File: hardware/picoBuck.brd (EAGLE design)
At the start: 22.8 x 27.3 mm, 26 parts, among them U1 AL8805, U2 AL8805, U3 AL8805

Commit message: Tweaks on text positions.
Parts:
- removed JP1: (no value), SparkFun:SCREWTERMINAL-3.5MM-3_LOCK.007S
- added JP3, JP4: M022.54MM_SCREWTERM, SparkFun-Connectors:1X02_2.54_SCREWTERM
- moved LOGO2 41.7 mm to (20.7, 2.16), flipped to the bottom
- moved LOGO1 39.0 mm to (9.02, 24.1), flipped to the bottom
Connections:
- net CTRL_CH1: now also JP4.P1; no longer JP1.3
- net CTRL_CH2: now also JP3.P2; no longer JP1.2
- net CTRL_CH3: now also JP3.P1; no longer JP1.1
- net GND: now also JP4.P2
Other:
- board text added: "GND"

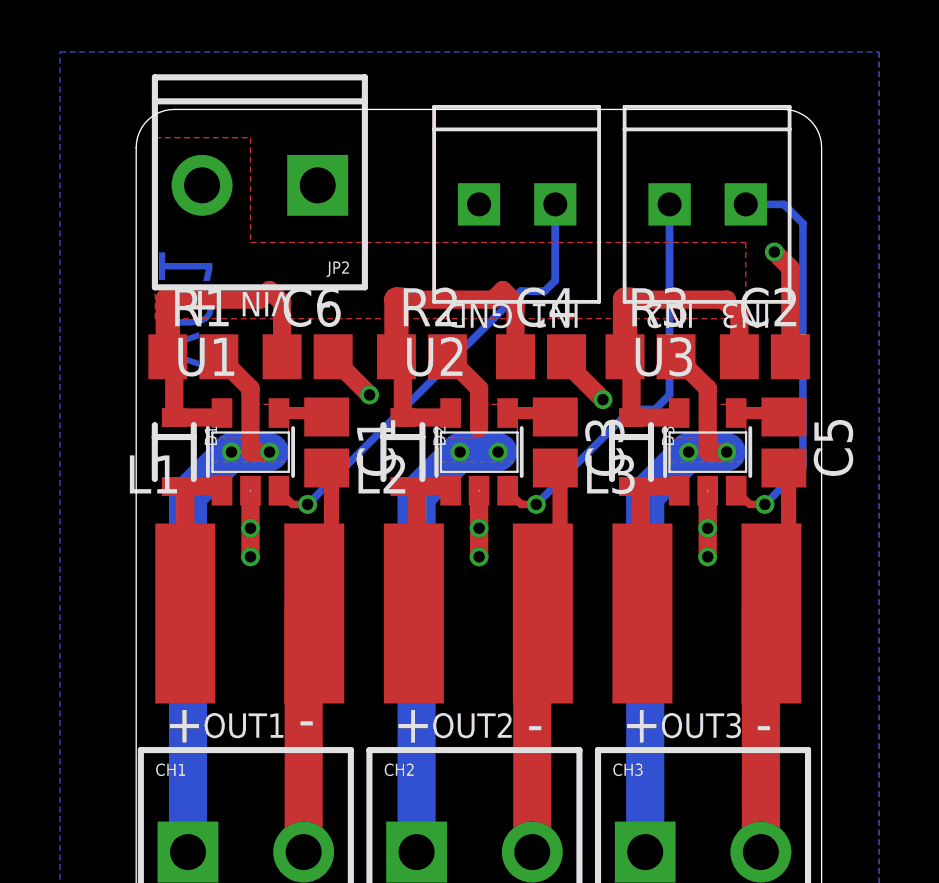
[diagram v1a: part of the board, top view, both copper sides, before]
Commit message: Update to v10, for release. Add .gitignore and README
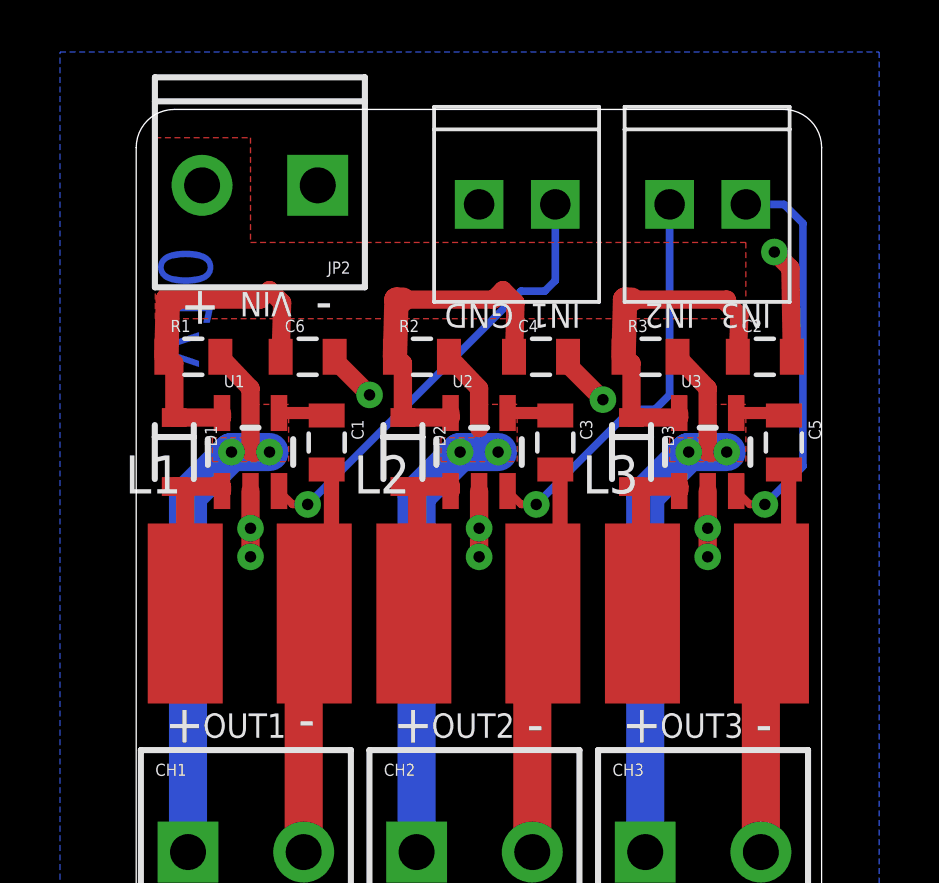
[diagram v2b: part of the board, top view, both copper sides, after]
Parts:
- C1, C2, C3, C4, C5, C6: device resistor:C0805 -> SparkFun-Capacitors:0805
- D1, D2, D3: device SparkFun:SOD-323 -> SparkFun-DiscreteSemi:SOD-323
- L1, L2, L3: value SRN6045 -> 33uH; device Protofusion:SRN6045 -> SparkFun-Passives:SRN6045
- R1, R2, R3: device resistor:R0805 -> SparkFun-Resistors:0805
- U1, U2, U3: value AL8805 -> (none); device Protofusion:SOT23-5 -> SparkFun-PowerIC:SOT23-5
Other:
- board text added: "v10"
- board text removed: "protofusion.org/picobuck"
- board text removed: "v01"

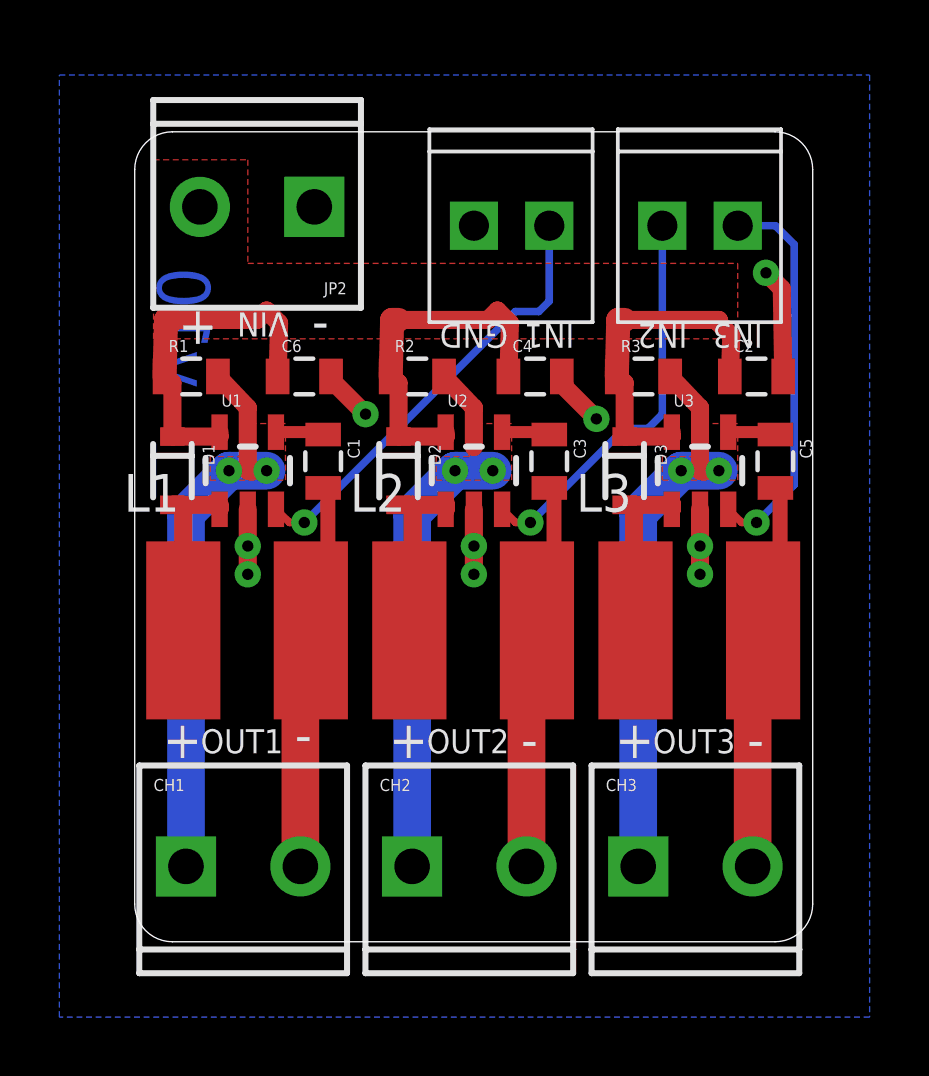
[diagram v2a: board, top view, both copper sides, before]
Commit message: Cosmetic tweaks
moved brd on grid, shrunk ground plane, other minor stuff
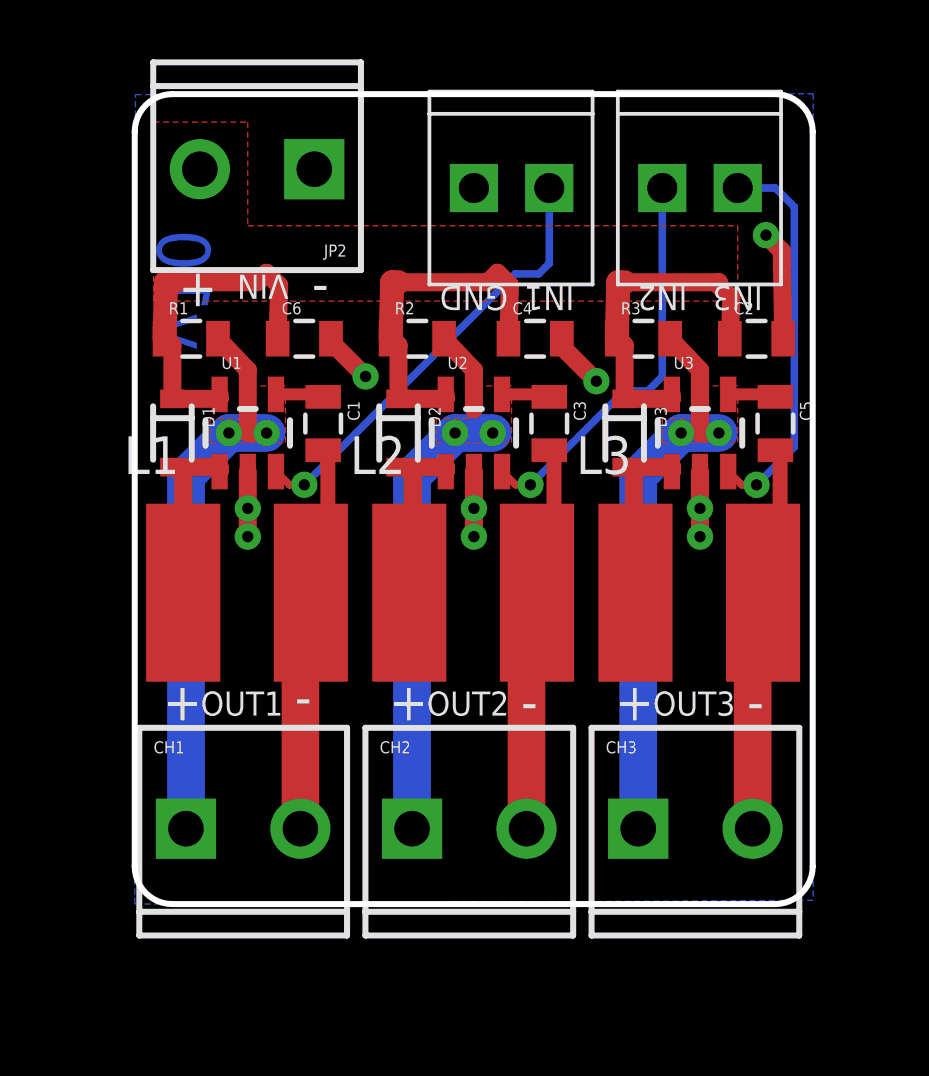
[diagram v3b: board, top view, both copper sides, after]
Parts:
- moved CH1 1.27 mm to (1.91, 2.54)
- moved CH2 1.27 mm to (9.53, 2.54)
- moved CH3 1.27 mm to (17.1, 2.54)
- moved LOGO2 1.27 mm to (20.7, 3.43)
- moved C1 1.27 mm to (6.35, 16.2)
- moved C2 1.27 mm to (21.0, 19.1)
- moved C3 1.27 mm to (14.0, 16.2)
- moved C4 1.27 mm to (13.5, 19.1)
- moved C5 1.27 mm to (21.6, 16.2)
- moved C6 1.27 mm to (5.71, 19.1)
- moved D1 1.27 mm to (1.27, 15.9)
- moved D2 1.27 mm to (8.89, 15.9)
- moved D3 1.27 mm to (16.5, 15.9)
- moved JP2 1.27 mm to (5.87, 24.8)
- moved JP3 1.27 mm to (17.8, 24.1)
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
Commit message: Production ready
panelized and added fiducials
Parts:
- added FID1, FID2: FIDUCIALUFIDUCIAL, SparkFun-Aesthetics:MICRO-FIDUCIAL
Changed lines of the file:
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@@
 <setting verticaltext="up"/>
 </settings>
-<grid distance="0.01" unitdist="inch" unit="inch" style="lines" multiple="1" display="yes" altdistance="0.001" altunitdist="inch" altunit="inch"/>
+<grid distance="0.05" unitdist="inch" unit="inch" style="lines" multiple="1" display="yes" altdistance="0.01" altunitdist="inch" altunit="inch"/>
 <layers>
 <layer number="1" name="Top" color="4" fill="1" visible="yes" active="yes"/>
@@
 <element name="JP3" library="SparkFun-Connectors" package="1X02_2.54_SCREWTERM" value="M022.54MM_SCREWTERM" x="17.78" y="24.13"/>
 <element name="JP4" library="SparkFun-Connectors" package="1X02_2.54_SCREWTERM" value="M022.54MM_SCREWTERM" x="11.43" y="24.13"/>
+<element name="FID1" library="SparkFun-Aesthetics" package="MICRO-FIDUCIAL" value="FIDUCIALUFIDUCIAL" x="3.81" y="1.016"/>
+<element name="FID2" library="SparkFun-Aesthetics" package="MICRO-FIDUCIAL" value="FIDUCIALUFIDUCIAL" x="20.828" y="25.908"/>
 </elements>
 <signals>

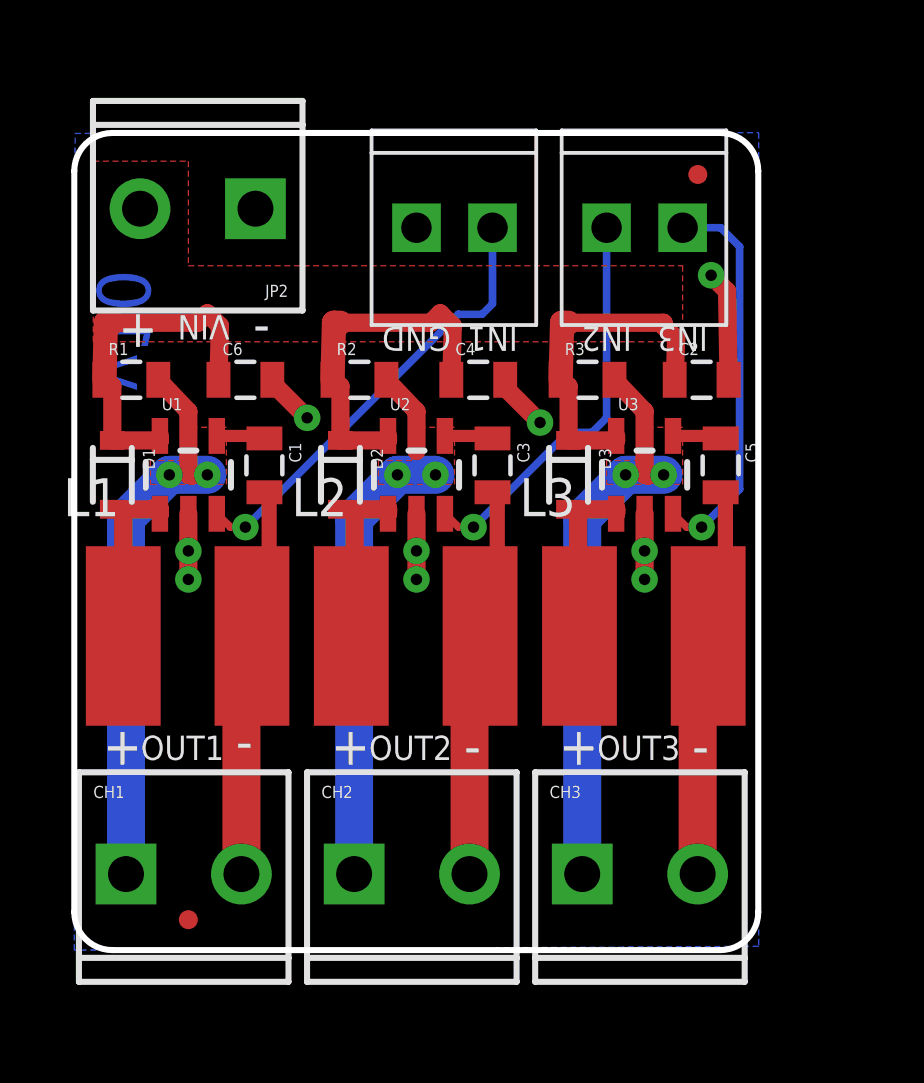
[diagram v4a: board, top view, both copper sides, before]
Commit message: High power initial revision - added 2nd sense resistor and solder jumper - changed diode to higher voltage version - changed input cap to higher voltage version
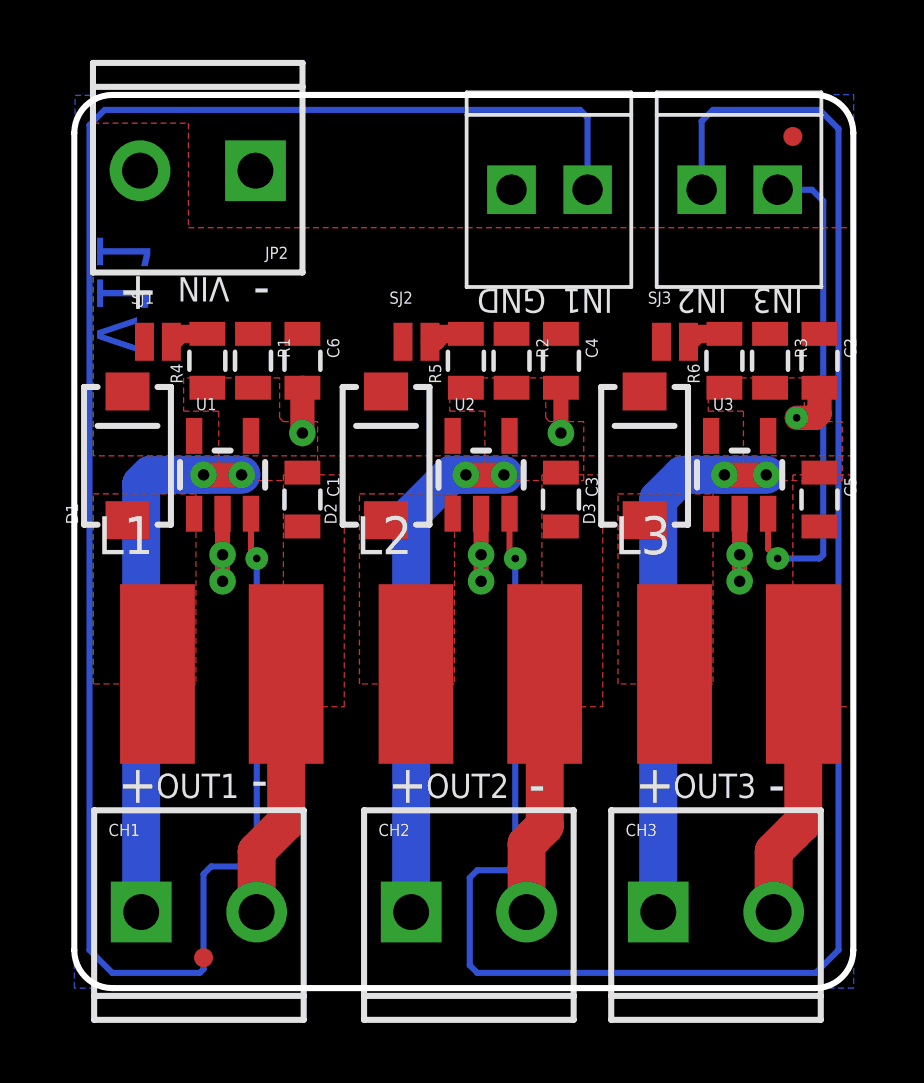
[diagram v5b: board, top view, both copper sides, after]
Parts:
- added R4, R5, R6: 0.3R, SparkFun-Resistors:0805
- added SJ1, SJ2, SJ3: JUMPER-PAD-2-NO, SparkFun-Passives:PAD-JUMPER-2-NO_NO_SILK
- D1, D2, D3: value BAT20JFILM -> MBRA140; device SparkFun-DiscreteSemi:SOD-323 -> SparkFun-DiscreteSemi:SMA-DIODE
- moved R3 6.13 mm to (23.2, 19.7), turned to 270 degrees
- moved R2 5.12 mm to (14.6, 19.7), turned to 270 degrees
- moved R1 4.11 mm to (5.97, 19.7), turned to 270 degrees
- moved C2 3.99 mm to (24.9, 19.7), turned to 270 degrees
- moved C5 3.49 mm to (24.9, 15.0)
- moved FID2 3.42 mm to (24.0, 27.2)
- moved JP4 3.42 mm to (14.6, 25.4)
- moved L3 3.42 mm to (22.2, 9.40)
- moved JP3 3.42 mm to (21.0, 25.4)
- moved U3 3.18 mm to (22.2, 15.9)
- moved CH3 2.84 mm to (19.7, 1.27)
- moved LOGO2 2.84 mm to (23.2, 2.16)
- moved C4 2.83 mm to (16.3, 19.7), turned to 270 degrees
- moved D3 2.62 mm to (19.1, 16.5), turned to 90 degrees
- moved C3 2.56 mm to (16.3, 15.0)
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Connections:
- removed net N$18: C5.1, CH3.1, R3.2, U3.4
- new net N$1: C5.1, CH3.1, R3.2, R6.1, U3.4
- new net N$2: R4.2, SJ1.2
- new net N$3: R5.2, SJ2.2
- new net N$7: R6.2, SJ3.2
- net IND1-1: now also D1.A; no longer D1.2
- net IND2-1: now also D2.A; no longer D2.2
- net IND3-1: now also D3.A; no longer D3.2
- net N$11: now also R4.1
- net N$13: now also R5.1
- net VIN: now also D1.C, D2.C, D3.C, SJ1.1, SJ2.1, SJ3.1; no longer D1.1, D2.1, D3.1
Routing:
- net CTRL_CH1: track 15.0 -> 67.9 mm
- net CTRL_CH2: track 13.4 -> 63.8 mm
- net VIN: track 34.9 -> 0.00 mm
- net N$18: track 21.0 -> 0.00 mm, vias 2 -> 0
- net N$1: track 0.00 -> 19.1 mm, vias 0 -> 2
- net IND1-1: track 6.61 -> 0.00 mm
- net IND2-1: track 6.21 -> 0.00 mm
- net IND3-1: track 6.18 -> 0.00 mm
- net N$16: track 13.8 -> 8.36 mm
- net N$5: track 13.7 -> 8.36 mm
- net N$9: track 13.5 -> 8.20 mm
- net CTRL_CH3: track 13.2 -> 16.7 mm
- net GND: track 14.0 -> 11.5 mm
- net N$11: track 21.0 -> 19.0 mm
- net N$7: track 0.00 -> 1.73 mm
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- added copper zone on layer 1, net IND1-1
- added copper zone on layer 1, net IND2-1
- added copper zone on layer 1, net IND3-1
- added copper zone on layer 1, net N$1
- added copper zone on layer 1, net N$16
- added copper zone on layer 1, net N$5
- added copper zone on layer 1, net N$9
- removed copper zone on layer 1, net N$18
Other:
- board size 22.8 x 27.3 mm -> 26 x 29.8 mm
- board text added: "v11"
- board text removed: "v10"

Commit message: Make files as they were before I started monkeying with them
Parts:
- added STANDOFF1, STANDOFF2: STAND-OFF, SparkFun-Electromechanical:STAND-OFF
- U1, U2, U3: value (none) -> AL8805
- moved FRAME1 12.6 mm to (11.4, -31.8)
- moved JP4 1.80 mm to (13.3, 26.7)
- moved CH2 1.33 mm to (11.0, 2.54)
- moved JP3 1.27 mm to (21.0, 26.7)
- moved C1 1.27 mm to (7.62, 16.3)
- moved C3 1.27 mm to (16.3, 16.3)
- moved C5 1.27 mm to (24.9, 16.3)
- moved CH1 1.27 mm to (2.41, 2.54)
- moved CH3 1.27 mm to (19.7, 2.54)
- moved FID1 1.27 mm to (4.32, 1.02)
- moved LOGO2 1.27 mm to (23.2, 3.43)
- moved C2 1.27 mm to (24.9, 21.0)
- moved C4 1.27 mm to (16.3, 21.0)
- moved C6 1.27 mm to (7.62, 21.0)
- moved D1 1.27 mm to (1.78, 17.8)
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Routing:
- net CTRL_CH1: track 67.9 -> 66.6 mm
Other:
- board size 26 x 29.8 mm -> 36.2 x 29.8 mm
- board text added: "#4-40 typ."
- board text added: "(typ.)"
- board text added: "Ethan Zonca/Mike Hord"
- board text added: "Units are inches"

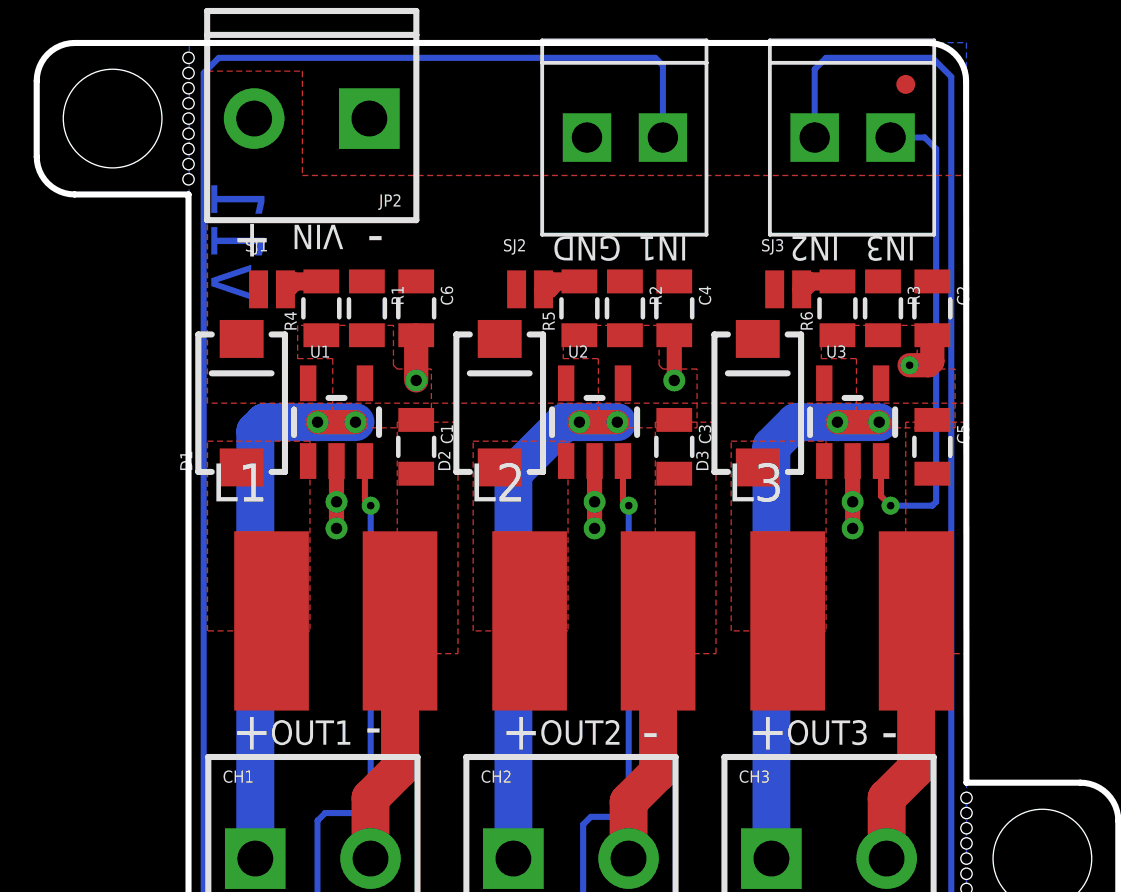
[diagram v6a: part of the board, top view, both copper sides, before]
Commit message: Updated library for some silk changes
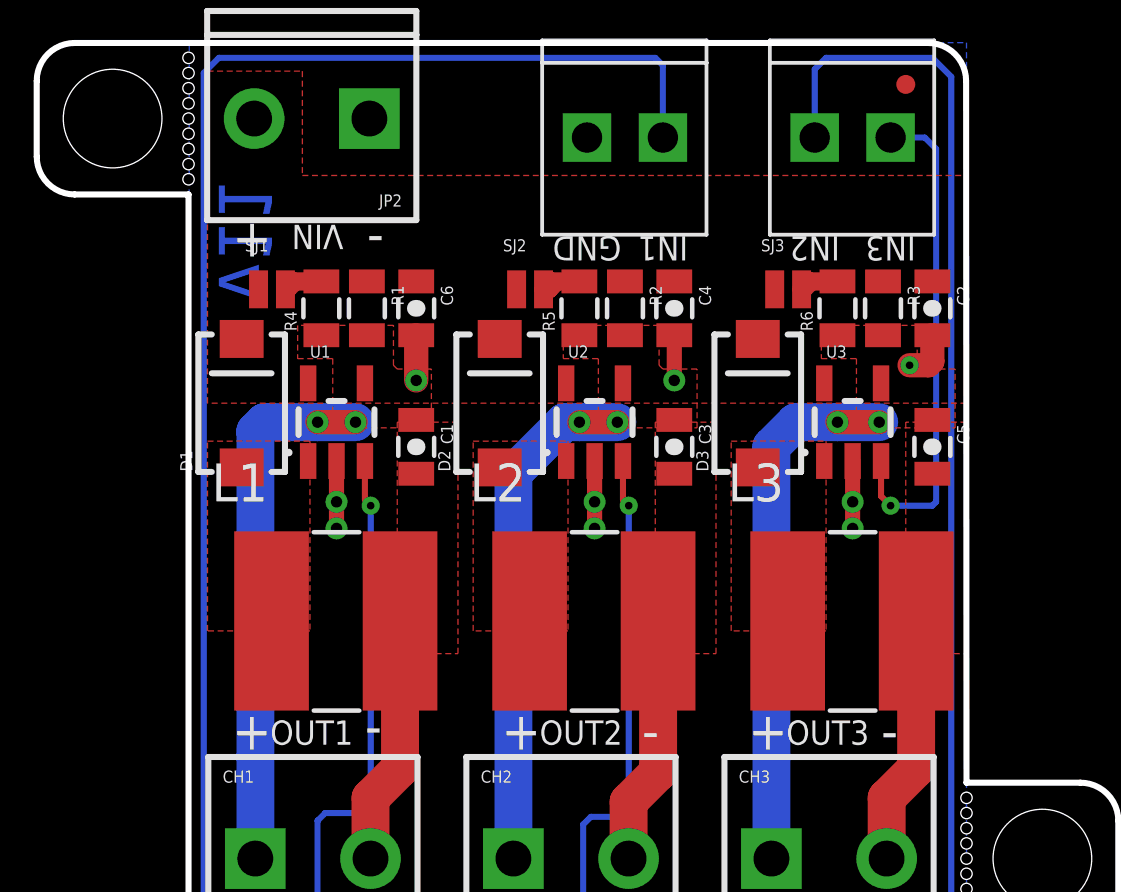
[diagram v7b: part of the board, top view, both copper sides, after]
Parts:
- C1, C3, C5: value 1uF -> 1.0uF; device SparkFun-Capacitors:0805 -> SparkFun-Capacitors:0805-CAP
- C2, C4, C6: device SparkFun-Capacitors:0805 -> SparkFun-Capacitors:0805-CAP
- R1, R2, R3, R4, R5, R6: value 0.3R -> 0.3
- U1, U2, U3: value AL8805 -> AL8805WS
